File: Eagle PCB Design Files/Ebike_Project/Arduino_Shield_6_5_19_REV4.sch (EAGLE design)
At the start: 31 parts, among them IC1 FT232RL, IC2 LM1117IMPX-5.0, IC3 328P-MUR, SW1 RESET, Y1 16MHz

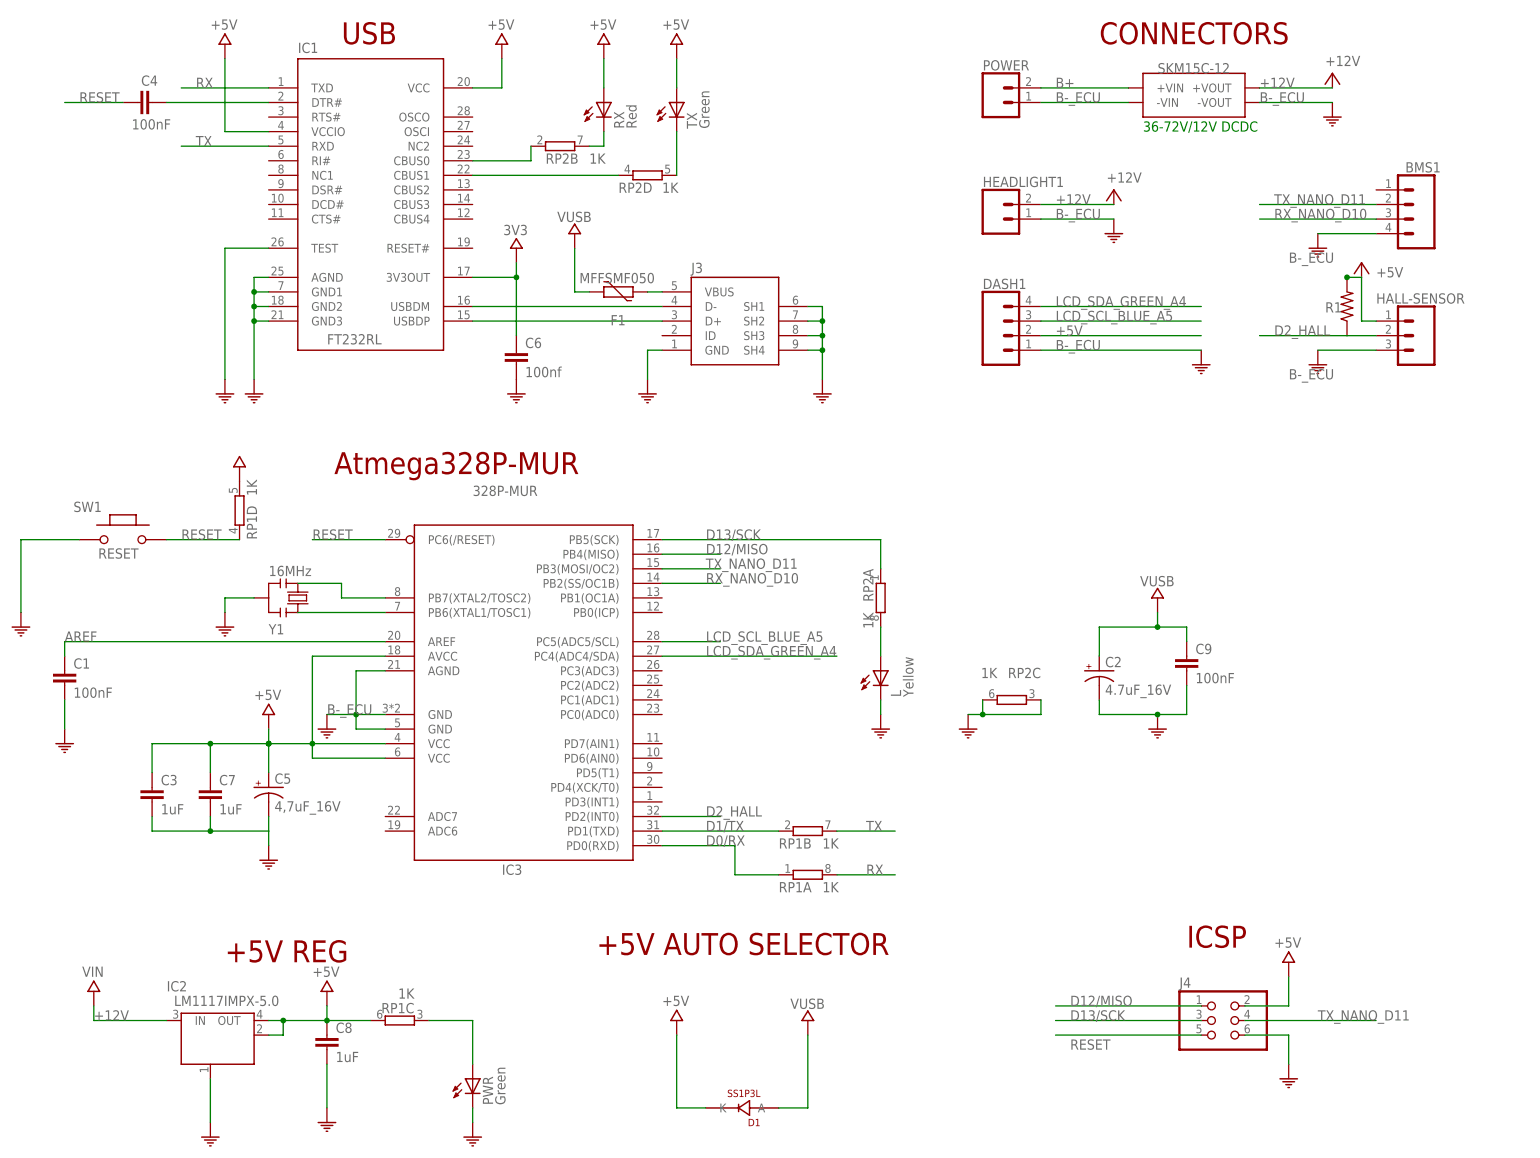
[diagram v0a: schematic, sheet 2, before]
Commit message: REV4 is Complete, PCB and BOM sent out
Evaluation of REV4 will be completed by the end of July
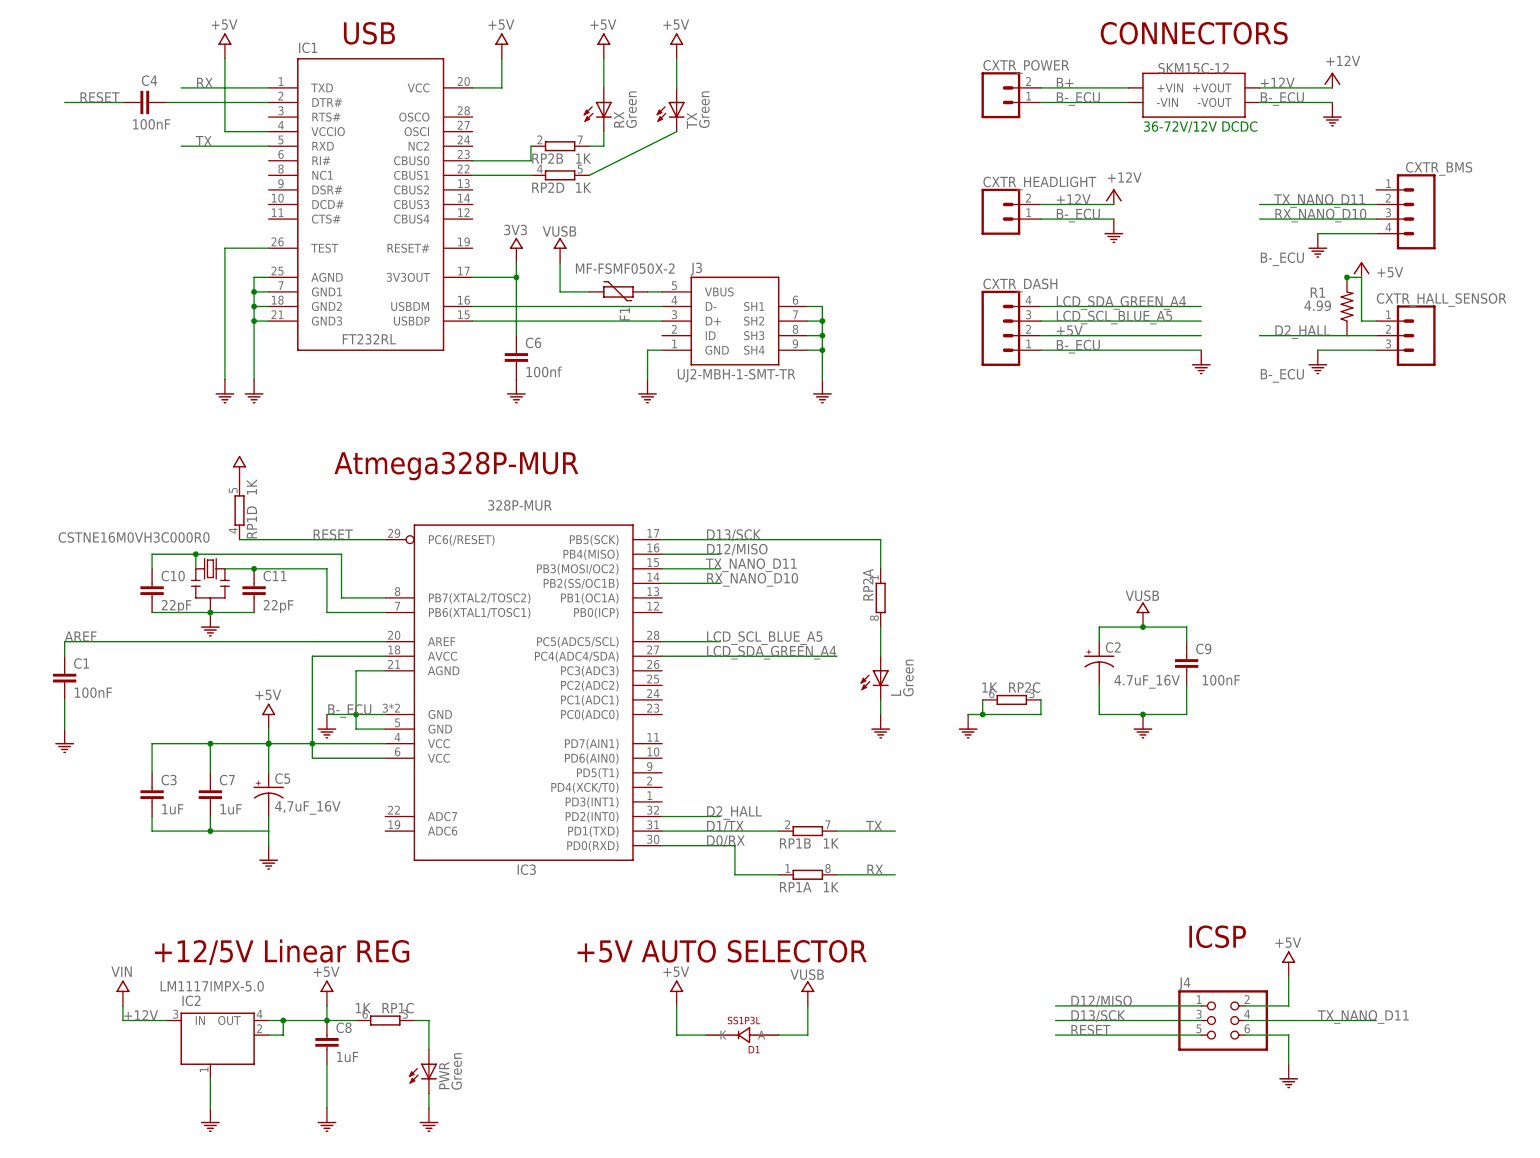
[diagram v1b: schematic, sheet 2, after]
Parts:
- removed SW1: RESET, Switches:0173_IT-1185AP1C-160G-G_T&R
- removed Y1: 16MHz, Cristalli:0011_CSTCE16M0V53-R0
- added C10, C11: 22pF, EBike_Project_Library:CAPACITOR_22PF
- added RESONATOR: CSTNE16M0VH3C000R0, EBike_Project_Library:RESONATOR
- D1: device Diodi:0025_SS1P3L-M3/84A -> EBike_Project_Library:SCHOTTKY_DIODE
- F1: value MFFSMF050 -> MF-FSMF050X-2; device Arduino-rcl:PTC -> EBike_Project_Library:FUSE_RESETTABLE
- IC1: device IntegratedCircuits:0226_FT232RL -> EBike_Project_Library:USB<>UART_IC
- IC2: device IntegratedCircuits:0022_LM1117IMPX-5.0 -> EBike_Project_Library:LINEAR_VREG
- IC3: device Arduino-ucs&SoCs:ATMEGA328P-32MUR -> EBike_Project_Library:ATMEGA328P_MURMUR
- J3: value (none) -> UJ2-MBH-1-SMT-TR; device Connettori:0219_14850 -> EBike_Project_Library:USB_MINI
- J4: device Connettori:0114_PH254-203DF118A00V -> EBike_Project_Library:2X3_.1"_ARRAY
- L: value Yellow -> Green; device Opto:0044_KPT-2012YC -> EBike_Project_Library:LED_GREEN
- PWR, TX: device Opto:0043_KPT-2012SGC -> EBike_Project_Library:LED_GREEN
- R1: value 0.3 -> 4.99; device EBike_Project_Library:RESISTOR_0805-0805-1/8W-1% -> EBike_Project_Library:RESISTOR_4.99K_0805-0805-1/8W-1%
- RP1, RP2: device Resistenze:0005_064R_1K_/_CAY16-102J4LF -> EBike_Project_Library:RESISTOR_ARRAY
- RX: value Red -> Green; device Opto:0181_KTP-2012SURCK -> EBike_Project_Library:LED_GREEN
- renumbered BMS1 to CXTR_BMS, DASH1 to CXTR_DASH, HALL-SENSOR to CXTR_HALL_SENSOR, HEADLIGHT1 to CXTR_HEADLIGHT, POWER to CXTR_POWER
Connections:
- removed net N$17: IC3.PB7(XTAL2/TOSC2), Y1.3
- new net N$20: C10.1, IC3.PB7(XTAL2/TOSC2), RESONATOR.3
- net B-_ECU: now also C10.2, C11.2, RESONATOR.2; no longer SW1.1, Y1.2
- net N$14: now also C11.1, RESONATOR.1; no longer Y1.1
- net RESET: no longer SW1.2
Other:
- note added: "+12/5V Linear REG"
- note removed: "+5V REG"
- moved on the sheet: C2, D1, PWR, RP1C, RP2D
